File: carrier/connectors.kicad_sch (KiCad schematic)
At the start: 9 parts, among them J5 USB_C_Receptacle_USB2.0, J6 USB_C_Receptacle_USB2.0

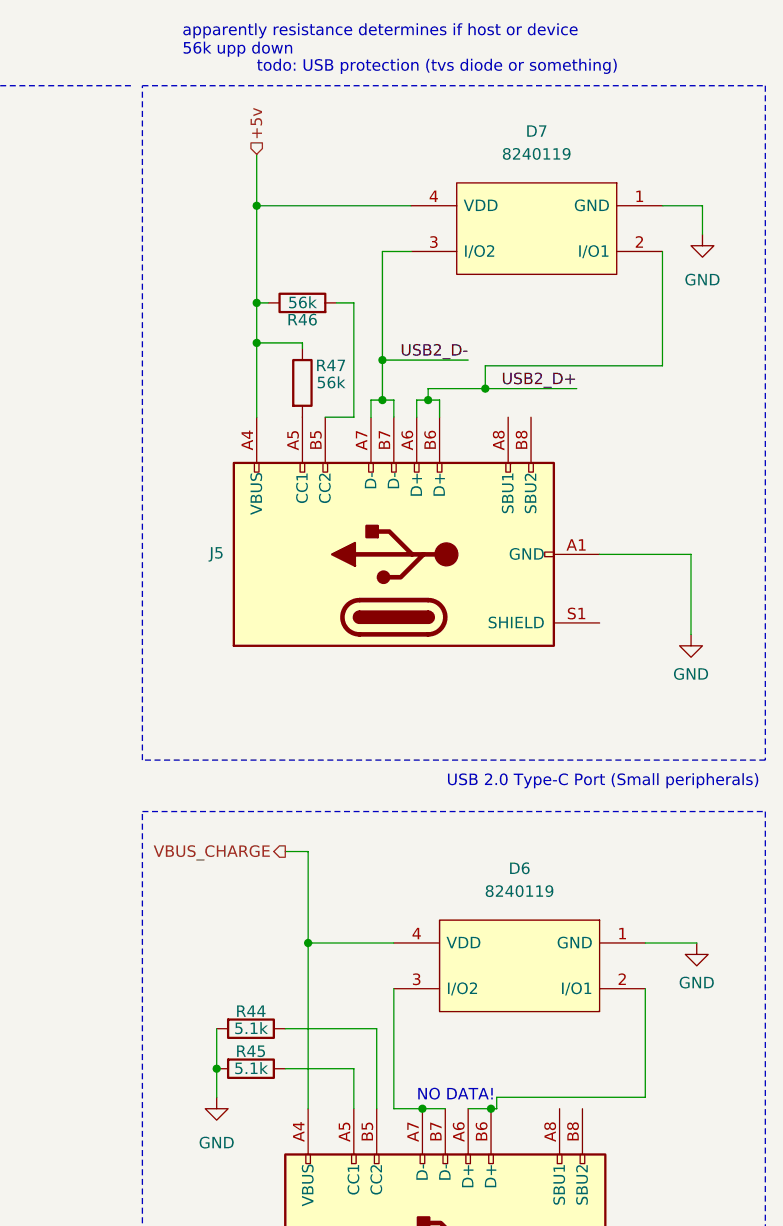
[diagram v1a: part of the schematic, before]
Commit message: new footprints - order stuff soon
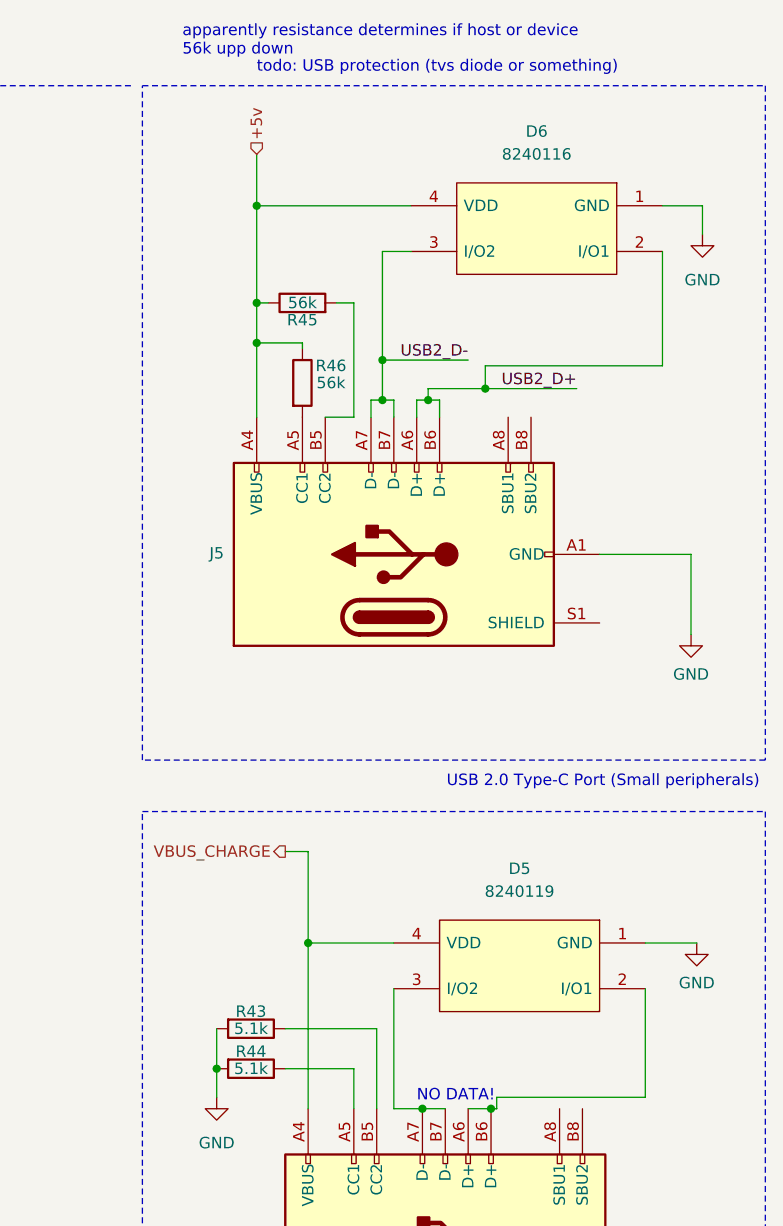
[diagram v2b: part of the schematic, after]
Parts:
- D5: renamed from D6; footprint CM4IO:SOT143-4L -> Package_TO_SOT_SMD:SOT-143R_Reverse_Handsoldering
- D6: renamed from D7; value 8240119 -> 8240116; footprint CM4IO:SOT143-4L -> Package_TO_SOT_SMD:SOT-143R_Reverse_Handsoldering
- J5, J6: footprint Connector_USB:USB_C_Receptacle_JAE_DX07S016JA1R1500 -> CM4IO:GCT_USB4510-03-1-A_REVA
- renumbered R44 to R43, R45 to R44, R46 to R45, R47 to R46
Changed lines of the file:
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@@
   (symbol (lib_id "Device:R") (at 227.33 121.92 270) (unit 1)
     (in_bom yes) (on_board yes)
-    (property "Reference" "R45" (id 0) (at 227.33 120.015 90))
+    (property "Reference" "R44" (id 0) (at 227.33 120.015 90))
     (property "Value" "5.1k" (id 1) (at 227.33 121.92 90))
     (property "Footprint" "Resistor_SMD:R_0603_1608Metric_Pad0.98x0.95mm_HandSolder" (id 2) (at 227.33 120.142 90)
@@
   (symbol (lib_id "Device:R") (at 233.045 45.72 0) (unit 1)
     (in_bom yes) (on_board yes)
-    (property "Reference" "R47" (id 0) (at 236.22 43.815 0))
+    (property "Reference" "R46" (id 0) (at 236.22 43.815 0))
     (property "Value" "56k" (id 1) (at 236.22 45.72 0))
     (property "Footprint" "Resistor_SMD:R_0805_2012Metric_Pad1.20x1.40mm_HandSolder" (id 2) (at 231.267 45.72 90)
@@
       (effects (font (size 1.27 1.27)) hide)
     )
-    (property "Footprint" "Connector_USB:USB_C_Receptacle_JAE_DX07S016JA1R1500" (id 2) (at 248.92 137.795 0)
+    (property "Footprint" "CM4IO:GCT_USB4510-03-1-A_REVA" (id 2) (at 248.92 137.795 0)
       (effects (font (size 1.27 1.27)) hide)
     )
@@
   (symbol (lib_id "Device:R") (at 227.33 117.475 270) (unit 1)
     (in_bom yes) (on_board yes)
-    (property "Reference" "R44" (id 0) (at 227.33 115.57 90))
+    (property "Reference" "R43" (id 0) (at 227.33 115.57 90))
     (property "Value" "5.1k" (id 1) (at 227.33 117.475 90))
     (property "Footprint" "Resistor_SMD:R_0603_1608Metric_Pad0.98x0.95mm_HandSolder" (id 2) (at 227.33 115.697 90)
@@
   (symbol (lib_id "tvs:8240119") (at 271.145 107.95 0) (mirror y) (unit 1)
     (in_bom yes) (on_board yes) (fields_autoplaced)
-    (property "Reference" "D6" (id 0) (at 257.175 99.695 0))
+    (property "Reference" "D5" (id 0) (at 257.175 99.695 0))
     (property "Value" "8240119" (id 1) (at 257.175 102.235 0))
-    (property "Footprint" "CM4IO:SOT143-4L" (id 2) (at 247.015 105.41 0)
+    (property "Footprint" "Package_TO_SOT_SMD:SOT-143R_Reverse_Handsoldering" (id 2) (at 247.015 105.41 0)
       (effects (font (size 1.27 1.27)) (justify left) hide)
     )
@@
       (effects (font (size 1.27 1.27)) hide)
     )
-    (property "Footprint" "Connector_USB:USB_C_Receptacle_JAE_DX07S016JA1R1500" (id 2) (at 243.205 60.96 0)
+    (property "Footprint" "CM4IO:GCT_USB4510-03-1-A_REVA" (id 2) (at 243.205 60.96 0)
       (effects (font (size 1.27 1.27)) hide)
     )
@@
   (symbol (lib_id "tvs:8240119") (at 273.05 26.035 0) (mirror y) (unit 1)
     (in_bom yes) (on_board yes) (fields_autoplaced)
-    (property "Reference" "D7" (id 0) (at 259.08 17.78 0))
-    (property "Value" "8240119" (id 1) (at 259.08 20.32 0))
-    (property "Footprint" "CM4IO:SOT143-4L" (id 2) (at 248.92 23.495 0)
+    (property "Reference" "D6" (id 0) (at 259.08 17.78 0))
+    (property "Value" "8240116" (id 1) (at 259.08 20.32 0))
+    (property "Footprint" "Package_TO_SOT_SMD:SOT-143R_Reverse_Handsoldering" (id 2) (at 248.92 23.495 0)
       (effects (font (size 1.27 1.27)) (justify left) hide)
     )
@@
   (symbol (lib_id "Device:R") (at 233.045 36.83 90) (unit 1)
     (in_bom yes) (on_board yes)
-    (property "Reference" "R46" (id 0) (at 233.045 38.735 90))
+    (property "Reference" "R45" (id 0) (at 233.045 38.735 90))
     (property "Value" "56k" (id 1) (at 233.045 36.83 90))
     (property "Footprint" "Resistor_SMD:R_0805_2012Metric_Pad1.20x1.40mm_HandSolder" (id 2) (at 233.045 38.608 90)

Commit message: buggy
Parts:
- removed Module2: ComputeModule4-CM4, CM4IO:Raspberry-Pi-4-Compute-Module, symbol CM4IO:ComputeModule4-CM4
- added Module1: ComputeModule4-CM4, CM4IO:Raspberry-Pi-4-Compute-Module, symbol CM4IO:ComputeModule4-CM4
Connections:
- net CLK_N: now also Module1.190 (HDMI0_CLK_N)
- net CLK_P: now also Module1.188 (HDMI0_CLK_P)
- net GND: now also Module1.101 (USB_OTG_ID), Module1.102 (PCIe_CLK_nREQ), Module1.107 (GND), Module1.108 (GND), Module1.110 (PCIe_CLK_P), Module1.112 (PCIe_CLK_N), Module1.113 (GND), Module1.114 (GND), Module1.116 (PCIe_RX_P), Module1.118 (PCIe_RX_N), Module1.119 (GND), Module1.120 (GND), Module1.122 (PCIe_TX_P), Module1.124 (PCIe_TX_N), Module1.125 (GND), Module1.126 (GND), Module1.128 (CAM0_D0_N), Module1.130 (CAM0_D0_P), Module1.131 (GND), Module1.132 (GND), Module1.134 (CAM0_D1_N), Module1.136 (CAM0_D1_P), Module1.137 (GND), Module1.138 (GND), Module1.140 (CAM0_C_N), Module1.142 (CAM0_C_P), Module1.144 (GND), Module1.146 (HDMI1_TX2_P), Module1.147 (HDMI1_SCL), Module1.148 (HDMI1_TX2_N), Module1.150 (GND), Module1.152 (HDMI1_TX1_P), Module1.154 (HDMI1_TX1_N), Module1.155 (GND), Module1.156 (GND), Module1.157 (DSI0_D0_N), Module1.158 (HDMI1_TX0_P), Module1.159 (DSI0_D0_P), Module1.160 (HDMI1_TX0_N), Module1.161 (GND), Module1.162 (GND), Module1.163 (DSI0_D1_N), Module1.164 (HDMI1_CLK_P), Module1.165 (DSI0_D1_P), Module1.166 (HDMI1_CLK_N), Module1.167 (GND), Module1.168 (GND), Module1.169 (DSI0_C_N), Module1.171 (DSI0_C_P), Module1.173 (GND), Module1.174 (GND), Module1.175 (DSI1_D0_N), Module1.177 (DSI1_D0_P), Module1.179 (GND), Module1.180 (GND), Module1.181 (DSI1_D1_N), Module1.183 (DSI1_D1_P), Module1.185 (GND), Module1.186 (GND), Module1.187 (DSI1_C_N), Module1.189 (DSI1_C_P), Module1.191 (GND), Module1.192 (GND), Module1.193 (DSI1_D2_N), Module1.194 (DSI1_D3_N), Module1.195 (DSI1_D2_P), Module1.196 (DSI1_D3_P), Module1.197 (GND), Module1.198 (GND)
- net HDMI_CEC: now also Module1.151 (HDMI0_CEC)
- net HDMI_HP: now also Module1.153 (HDMI0_HOTPLUG)
- net HDMI_SCL: now also Module1.200 (HDMI0_SCL)
- net HDMI_SDA: now also Module1.199 (HDMI0_SDA)
- net TX0_N: now also Module1.184 (HDMI0_TX0_N)
- net TX0_P: now also Module1.182 (HDMI0_TX0_P)
- net TX1_N: now also Module1.178 (HDMI0_TX1_N)
- net TX1_P: now also Module1.176 (HDMI0_TX1_P)
- net TX2_N: now also Module1.172 (HDMI0_TX2_N)
- net TX2_P: now also Module1.170 (HDMI0_TX2_P)
- net USB2_D+: now also Module1.105 (USB2_P)
- net USB2_D-: now also Module1.103 (USB2_N)

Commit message: chrgere
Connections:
- net pwr_CC1: now reaches J6.A5 (CC1), R44.1
- net pwr_DP: now reaches D5.2 (I/O1), J6.A6 (D+), J6.B6 (D+)
- net pwr_DN: now reaches D5.3 (I/O2), J6.A7 (D-), J6.B7 (D-)
- net pwr_CC2: now reaches J6.B5 (CC2), R43.1
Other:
- note removed: "NO DATA!"
